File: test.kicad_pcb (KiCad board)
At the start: 2 copper layers, 139.2 x 72.4 mm, 60 parts, among them J1 USB_C_Receptacle_USB2.0_16P, J2 Conn_01x02_Pin (switch), J3 Conn_01x02_Pin (battery), J4 Conn_01x03_Pin, SW1 SW_Push, SW10 SW_Push, SW11 SW_Push, SW12 SW_Push, SW13 SW_Push, SW14 SW_Push, SW15 SW_Push, SW16 SW_Push, SW17 SW_Push, SW18 SW_Push, SW19 SW_Push, SW2 SW_Push, SW3 SW_Push, SW4 SW_Push, SW5 SW_Push, SW6 SW_Push, SW7 SW_Push, SW8 SW_Push, SW9 SW_Push, U1 E73-2G4M08S1C, U2 AP2112K-3.3, U3 MCP73831-2-OT, U4 USBLC6-2SC6

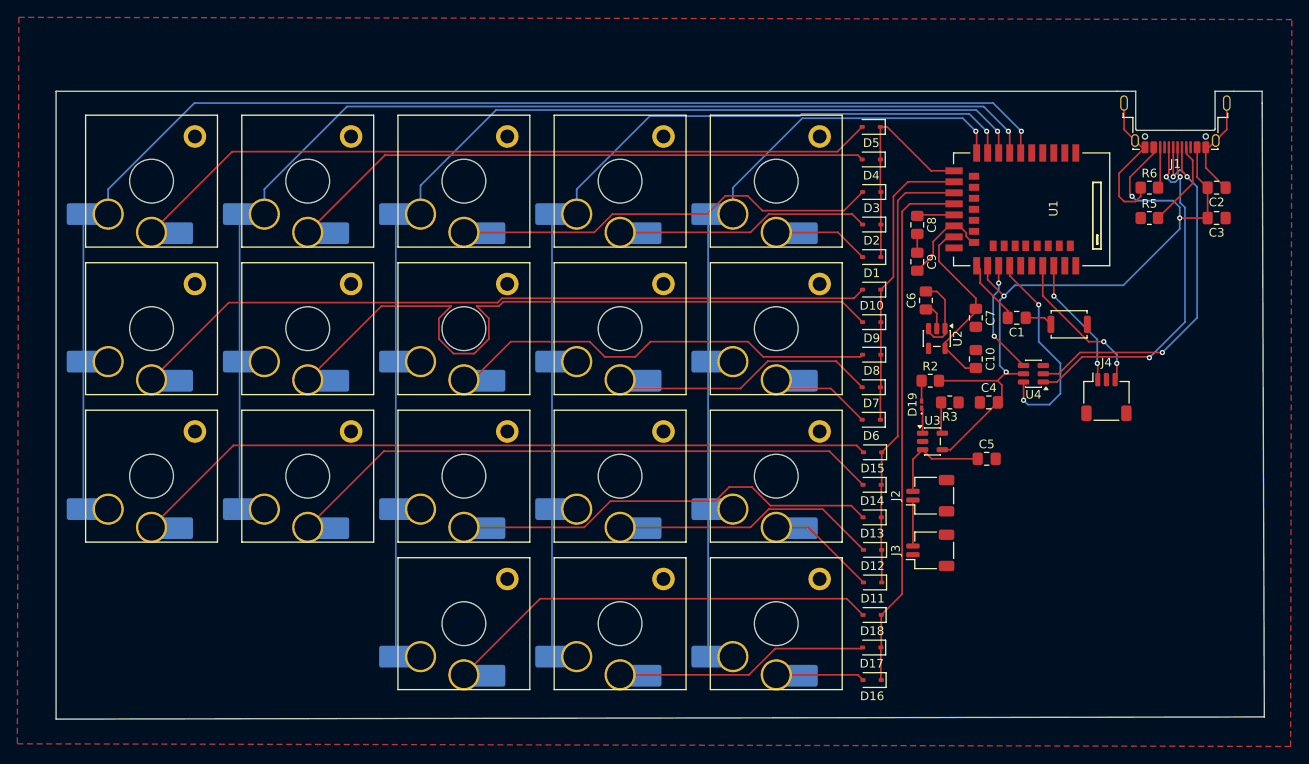
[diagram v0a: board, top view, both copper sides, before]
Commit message: feat(pcb): adding deps to get no error
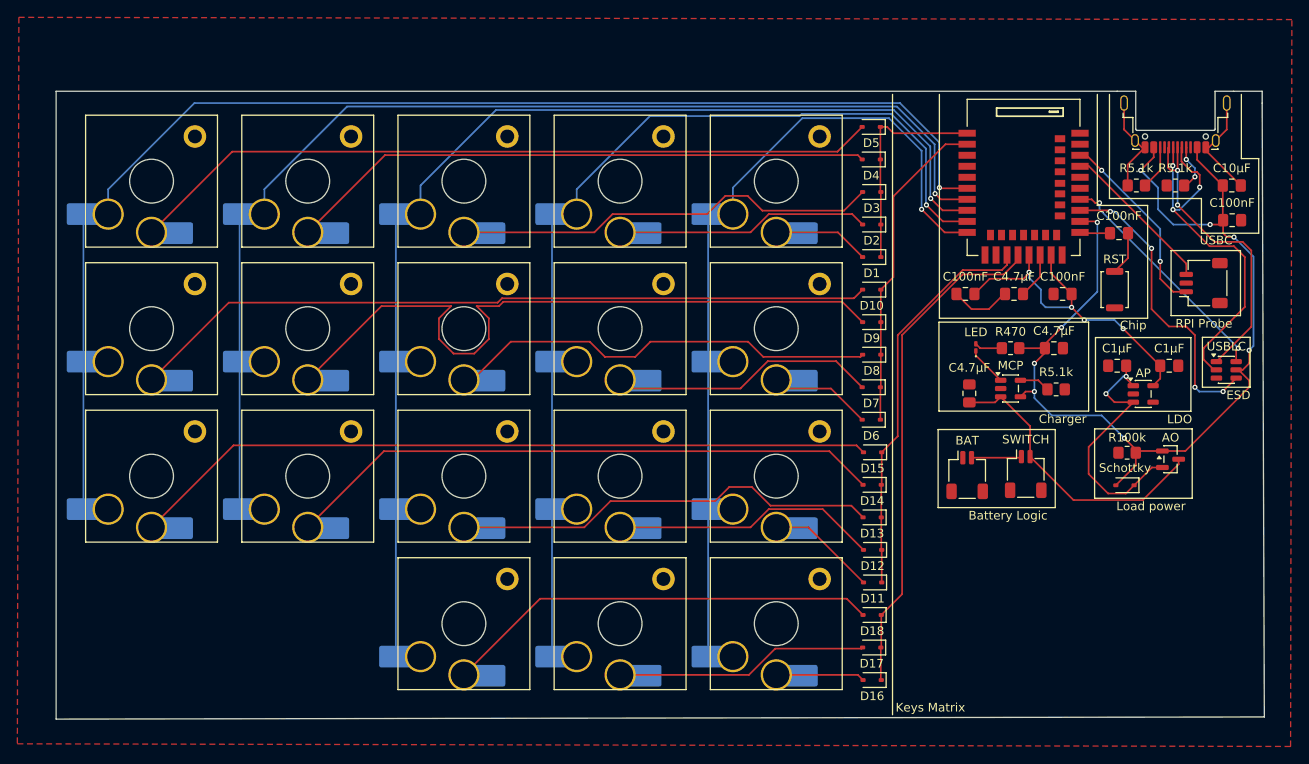
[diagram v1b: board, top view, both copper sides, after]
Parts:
- removed C1, C10, C3, C8: C (100nF), Capacitor_SMD:C_0805_2012Metric_Pad1.18x1.45mm_HandSolder
- removed C2: C (10µF), Capacitor_SMD:C_0805_2012Metric_Pad1.18x1.45mm_HandSolder
- removed C4, C5, C9: C (4.7µF), Capacitor_SMD:C_0805_2012Metric_Pad1.18x1.45mm_HandSolder
- removed C6, C7: C (1µF), Capacitor_SMD:C_0805_2012Metric_Pad1.18x1.45mm_HandSolder
- removed D19: LED, LED_SMD:LED_0201_0603Metric_Pad0.64x0.40mm_HandSolder
- removed J2: Conn_01x02_Pin (switch), Connector_JST:JST_SH_SM02B-SRSS-TB_1x02-1MP_P1.00mm_Horizontal
- removed J3: Conn_01x02_Pin (battery), Connector_JST:JST_SH_SM02B-SRSS-TB_1x02-1MP_P1.00mm_Horizontal
- removed R2: R (470), Resistor_SMD:R_0805_2012Metric_Pad1.20x1.40mm_HandSolder
- removed R3: R (5k), Resistor_SMD:R_0805_2012Metric_Pad1.20x1.40mm_HandSolder
- removed R5, R6: R (5.1k), Resistor_SMD:R_0805_2012Metric_Pad1.20x1.40mm_HandSolder
- removed SW19: SW_Push, Button_Switch_SMD:SW_Push_SPST_NO_Alps_SKRK
- removed U2: AP2112K-3.3, Package_TO_SOT_SMD:SOT-23-5
- removed U3: MCP73831-2-OT, Package_TO_SOT_SMD:SOT-23-5
- removed U4: USBLC6-2SC6, Package_TO_SOT_SMD:SOT-23-6
- added AO: AO3401A, Package_TO_SOT_SMD:SOT-23, F.Cu at (219.4, 103.0)
- added AP: AP2112K-3.3, Package_TO_SOT_SMD:SOT-23-5, F.Cu at (216.3, 95.5)
- added BAT: Conn_01x02_Pin (battery), Connector_JST:JST_SH_SM02B-SRSS-TB_1x02-1MP_P1.00mm_Horizontal, F.Cu at (196.0, 104.9)
- added C100nF: C (100nF), Capacitor_SMD:C_0805_2012Metric_Pad1.18x1.45mm_HandSolder, F.Cu at (226.5, 75.5)
- added C100nF: C (100nF), Capacitor_SMD:C_0805_2012Metric_Pad1.18x1.45mm_HandSolder, F.Cu at (207.0, 84.0)
- added C100nF: C (100nF), Capacitor_SMD:C_0805_2012Metric_Pad1.18x1.45mm_HandSolder, F.Cu at (213.5, 77.0)
- added C100nF: C (100nF), Capacitor_SMD:C_0805_2012Metric_Pad1.18x1.45mm_HandSolder, F.Cu at (195.8, 84.0)
- added C10µF: C (10µF), Capacitor_SMD:C_0805_2012Metric_Pad1.18x1.45mm_HandSolder, F.Cu at (226.5, 71.5)
- added C1µF: C (1µF), Capacitor_SMD:C_0805_2012Metric_Pad1.18x1.45mm_HandSolder, F.Cu at (213.3, 92.3)
- added C1µF: C (1µF), Capacitor_SMD:C_0805_2012Metric_Pad1.18x1.45mm_HandSolder, F.Cu at (219.3, 92.3)
- added C4.7µF: C (4.7µF), Capacitor_SMD:C_0805_2012Metric_Pad1.18x1.45mm_HandSolder, F.Cu at (201.4, 84.0)
- added C4.7µF: C (4.7µF), Capacitor_SMD:C_0805_2012Metric_Pad1.18x1.45mm_HandSolder, F.Cu at (196.2, 95.5)
- added C4.7µF: C (4.7µF), Capacitor_SMD:C_0805_2012Metric_Pad1.18x1.45mm_HandSolder, F.Cu at (206.0, 90.2)
- added LED: LED, LED_SMD:LED_0201_0603Metric_Pad0.64x0.40mm_HandSolder, F.Cu at (197.0, 90.2)
- added MCP: MCP73831-2-OT, Package_TO_SOT_SMD:SOT-23-5, F.Cu at (201.0, 94.9)
- added R100k: R (100k), Resistor_SMD:R_0805_2012Metric_Pad1.20x1.40mm_HandSolder, F.Cu at (214.4, 102.3)
- added R470: R (470), Resistor_SMD:R_0805_2012Metric_Pad1.20x1.40mm_HandSolder, F.Cu at (201.0, 90.2)
- added R5.1k: R (5.1k), Resistor_SMD:R_0805_2012Metric_Pad1.20x1.40mm_HandSolder, F.Cu at (220.0, 71.5)
- added R5.1k: R (5k), Resistor_SMD:R_0805_2012Metric_Pad1.20x1.40mm_HandSolder, F.Cu at (206.2, 95.0)
- added R5.1k: R (5.1k), Resistor_SMD:R_0805_2012Metric_Pad1.20x1.40mm_HandSolder, F.Cu at (215.5, 71.5)
- added RST: SW_Push, Button_Switch_SMD:SW_Push_SPST_NO_Alps_SKRK, F.Cu at (213.0, 83.5)
- added SWITCH: Conn_01x02_Pin (switch), Connector_JST:JST_SH_SM02B-SRSS-TB_1x02-1MP_P1.00mm_Horizontal, F.Cu at (202.8, 104.8)
- added Schottky: D_Schottky, Diode_SMD:D_SOD-323, F.Cu at (214.2, 106.0)
- added USBLC: USBLC6-2SC6, Package_TO_SOT_SMD:SOT-23-6, F.Cu at (225.9, 92.8)
- moved J4 17.3 mm to (223.2, 82.8), turned to 90 degrees
- moved U1 2.02 mm to (202.5, 72.5), turned to 180 degrees
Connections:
- U1 pad 1: unconnected-(U1-P1.11*-Pad1) -> row_1
- U1 pad 11: row_1 -> unconnected-(U1-P0.00/XL1-Pad11)
- U1 pad 13: row_2 -> unconnected-(U1-P0.01/XL2-Pad13)
- U1 pad 19: Net-(U1-VDD) -> 3v3
- U1 pad 2: unconnected-(U1-P1.10*-Pad2) -> row_2
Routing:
- net VBUS: track 86.1 -> 115.4 mm, vias 4 -> 9
- net D- (post-ESD): track 13.2 -> 34.9 mm, vias 2 -> 4
- net BAT: track 12.0 -> 33.7 mm
- net VSYS: track 9.22 -> 30.4 mm, vias 0 -> 2
- net 3v3: track 21.7 -> 39.9 mm, vias 0 -> 4
- net GND: track 42.9 -> 29.2 mm
- net D+ (pre-ESD): track 45.4 -> 35.4 mm, vias 3 -> 2
- net SWDCLK: track 15.2 -> 22.1 mm
- net row_3: track 51.7 -> 46.4 mm
- net col_1: track 88.5 -> 93.8 mm
- net Net-(C8-Pad2): track 2.17 -> 7.05 mm
- net Net-(U1-VDD): track 4.29 -> 0.00 mm
- net Net-(J1-CC1): track 10.1 -> 5.90 mm, vias 0 -> 2
- net Net-(U1-P0.18/RESET): track 7.48 -> 3.50 mm
- net row_2: track 34.1 -> 37.4 mm
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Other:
- board text added: "Battery Logic"
- board text added: "Charger"
- board text added: "Chip"
- board text added: "ESD"
- board text added: "Keys Matrix"
- board text added: "LDO"
- board text added: "Load power"
- board text added: "RPI Probe"
- board text added: "USBC"
